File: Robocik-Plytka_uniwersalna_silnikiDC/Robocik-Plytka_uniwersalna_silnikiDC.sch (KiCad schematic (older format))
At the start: 48 parts, among them IC1 ACSL-6400-00TE, IC3 L6205D, J1 Conn_01x02, J2 ENG, J3 Conn_01x02, Q1 Q_NPN_BCE, Q2 Q_NPN_BCE, Q3 Q_NPN_BCE, U1 STM32F103C8Tx, U2 LD1117S33TR_SOT223, U3 L78L05_SOT89

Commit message: Added CAN transceiver schematic, Boot and LSE/OSC oscillator schematic, updated drawing. Added MCU pinout from STM32CubeMX
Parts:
- added C? (x4): 100nF, symbol Device:C_Small
- added J2: Tryb, Connector_PinHeader_2.54mm:PinHeader_1x03_P2.54mm_Vertical, symbol Connector:Conn_01x03_Male
- added J3: Magistrala_CAN, Connector_PinHeader_2.54mm:PinHeader_1x02_P2.54mm_Vertical, symbol Connector:Conn_01x02_Male
- added JP1: Zworka, Connector_PinHeader_2.54mm:PinHeader_1x02_P2.54mm_Vertical, symbol Device:Jumper_NO_Small
- added R1: 10k, Resistor_SMD:R_1206_3216Metric, symbol Device:R_Small
- added R2: 2k2, Resistor_SMD:R_1206_3216Metric, symbol Device:R_Small
- added R3: 120R, Resistor_SMD:R_1206_3216Metric, symbol Device:R
- added R? (x4): 10k, symbol Device:R_Small
- added SW?: SW_SPDT, symbol Switch:SW_SPDT
- added U1: SN65HVD230, Package_SO:SOIC-8_3.9x4.9mm_P1.27mm, symbol Interface_CAN_LIN:SN65HVD230
- added Y?: HSE OSC, symbol Device:Crystal_Small
- added Y?: LSE OSC, symbol Device:Crystal_Small
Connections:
- net labels added: BOOT0, GND, Pin_D, Pin_R
- wire segments 166 -> 213
- no-connect marks 0 -> 2
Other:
- note added: "Terminator podłączany na początku i na końcu magistrali"
- moved on the sheet: C?, R?

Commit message: Changed transceiver ground to digital, fixed power ground labelson driver ground, added footprints for capacitors and resistors.
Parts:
- C1, C10, C11, C12, C2, C3, C4, C5, C6, C7, C8, C9: renamed from C?; footprint (none) -> Capacitor_SMD:C_1206_3216Metric
- C13: renamed from C7; footprint (none) -> Capacitor_SMD:C_1206_3216Metric
- C14: renamed from C8; footprint (none) -> Capacitor_SMD:C_1206_3216Metric
- C15: renamed from C11; footprint (none) -> Capacitor_SMD:C_1206_3216Metric
- C16: renamed from C4; footprint (none) -> Capacitor_SMD:C_1206_3216Metric
- C17: renamed from C3; footprint (none) -> Capacitor_SMD:C_1206_3216Metric
- C18: renamed from C9; footprint (none) -> Capacitor_SMD:C_1206_3216Metric
- C19: renamed from C5; footprint (none) -> Capacitor_SMD:C_1206_3216Metric
- C20: renamed from C10; footprint (none) -> Capacitor_SMD:C_1206_3216Metric
- C21: renamed from C1; footprint (none) -> Capacitor_SMD:C_1206_3216Metric
- C22: renamed from C2; footprint (none) -> Capacitor_SMD:CP_Elec_6.3x5.8
- C23: renamed from C6; footprint (none) -> Capacitor_SMD:C_1206_3216Metric
- C24: renamed from C12; footprint (none) -> Capacitor_SMD:C_1206_3216Metric
- D1, D2: footprint (none) -> Diode_SMD:D_SOD-123
- R1, R14, R15, R17, R2, R3, R4, R5: renamed from R?; footprint (none) -> Resistor_SMD:R_1206_3216Metric
- R11: renamed from R9; footprint (none) -> Resistor_SMD:R_1206_3216Metric
- R12: renamed from R10; footprint (none) -> Resistor_SMD:R_1206_3216Metric
- R13: renamed from R11; footprint (none) -> Resistor_SMD:R_1206_3216Metric
- R19: renamed from R16; footprint (none) -> Resistor_SMD:R_1206_3216Metric
- R20: renamed from R15; footprint (none) -> Resistor_SMD:R_1206_3216Metric
- R21: renamed from R17; footprint (none) -> Resistor_SMD:R_1206_3216Metric
- R6: renamed from R1; footprint (none) -> Resistor_SMD:R_1206_3216Metric
- R7: renamed from R2; footprint (none) -> Resistor_SMD:R_1206_3216Metric
- R8: renamed from R5; footprint (none) -> Resistor_SMD:R_1206_3216Metric
- R9: renamed from R6; footprint (none) -> Resistor_SMD:R_1206_3216Metric
- gave numbers to parts that had none: 4
- renumbered IC3 to IC2, J2 to J1, J1 to J4, J2 to J5, J3 to J6, R2 to R10, R1 to R16, R3 to R18, U1 to U2, U2 to U3, U3 to U4
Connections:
- net labels removed: GND, VssPWR
- wire segments 213 -> 218
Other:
- moved on the sheet: C21, C22

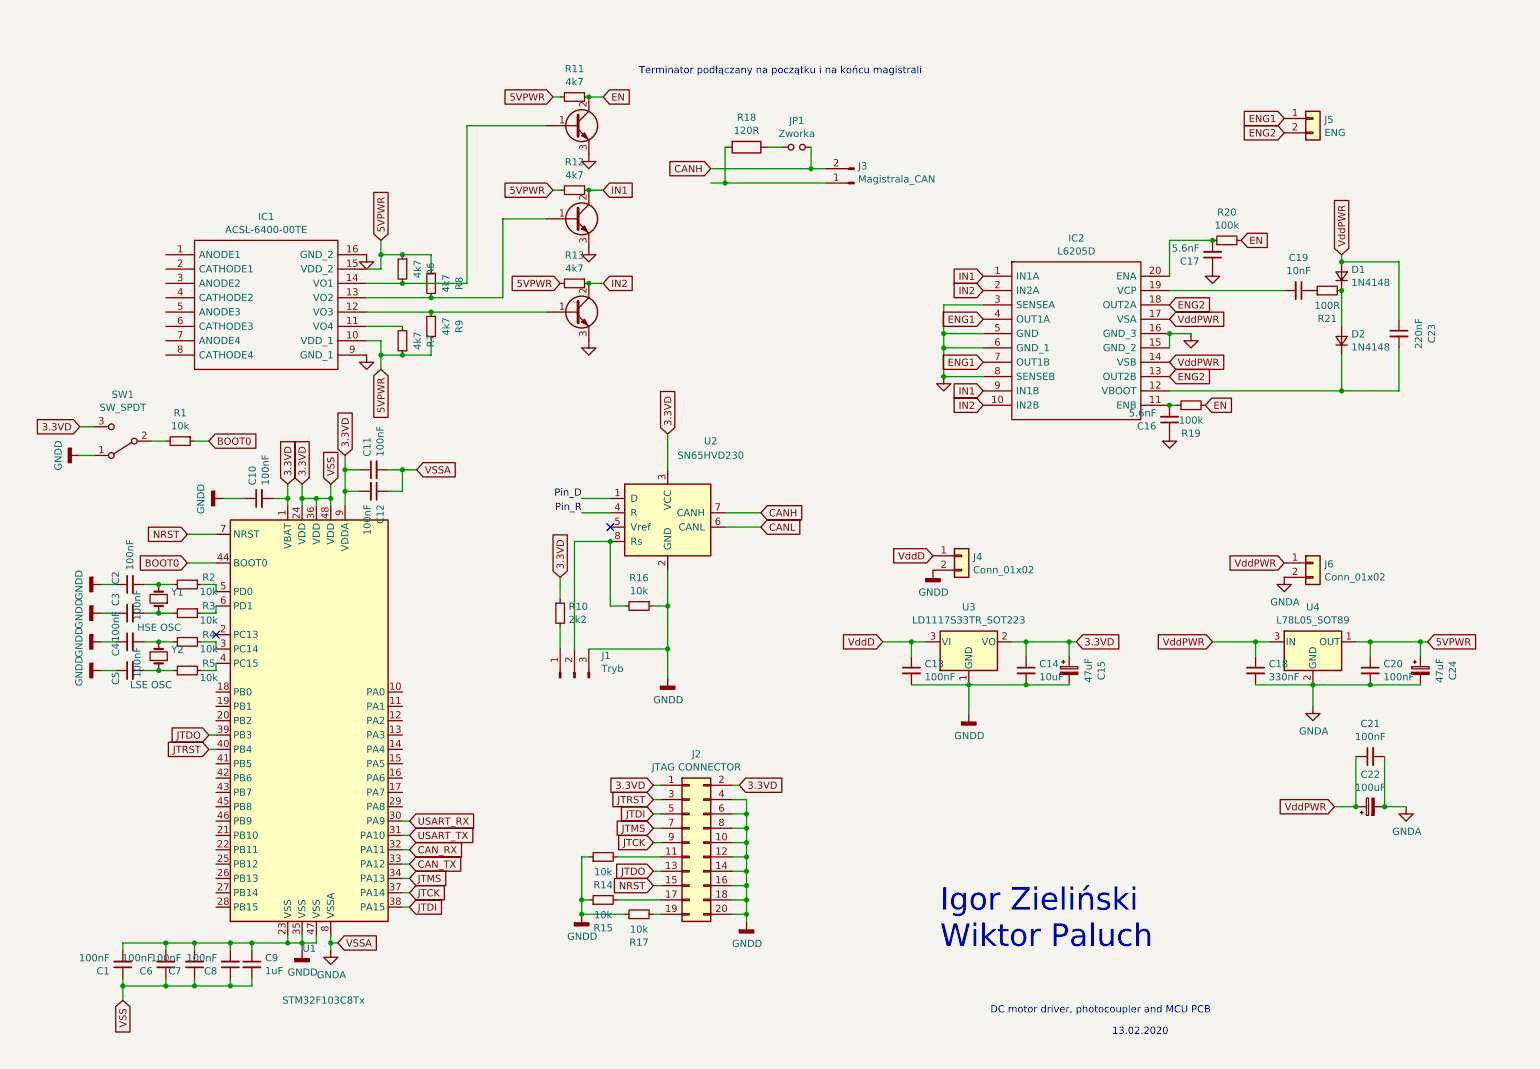
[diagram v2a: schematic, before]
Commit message: Schematic: Changed programming from JTAG to SWD. Added solderbridges. Added timers and their connections with optocoupler. Corrected minor mistakes. PCB: First version: organised elements, most connections are done.
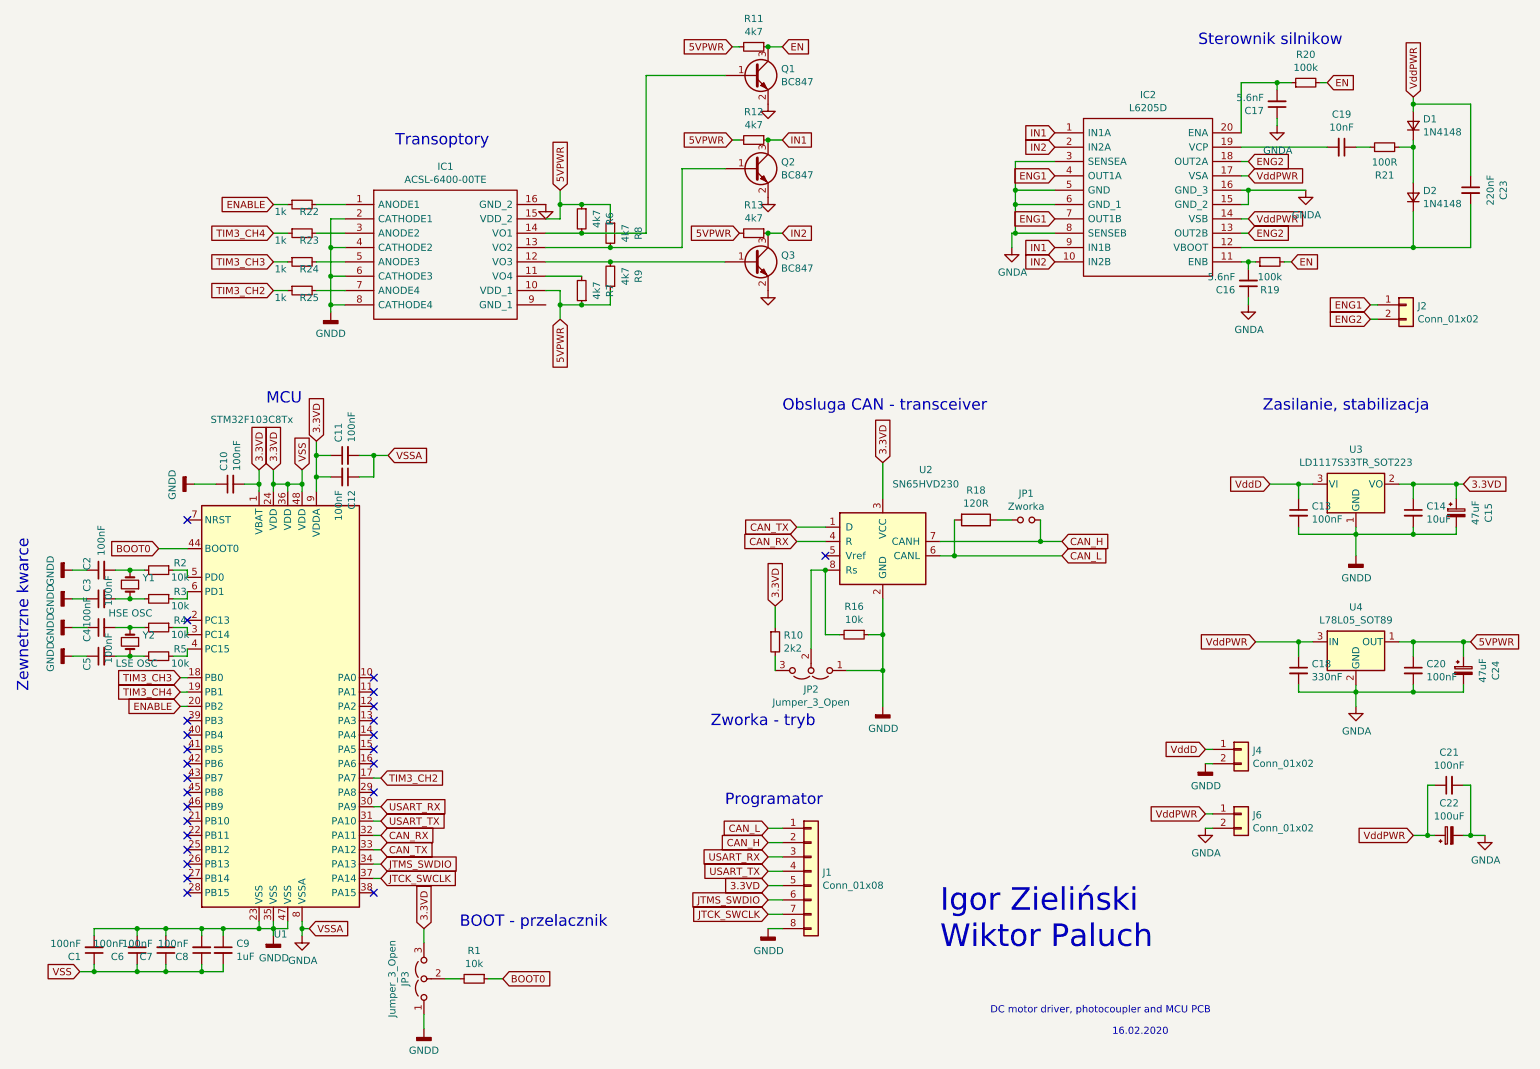
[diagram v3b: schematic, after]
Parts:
- removed J1: Tryb, Connector_PinHeader_2.54mm:PinHeader_1x03_P2.54mm_Vertical, symbol Connector:Conn_01x03_Male
- removed J2: JTAG CONNECTOR, symbol Connector_Generic:Conn_02x10_Odd_Even
- removed J3: Magistrala_CAN, Connector_PinHeader_2.54mm:PinHeader_1x02_P2.54mm_Vertical, symbol Connector:Conn_01x02_Male
- removed J5: ENG, symbol Connector_Generic:Conn_01x02
- removed Q1, Q2, Q3: Q_NPN_BCE, symbol Device:Q_NPN_BCE
- removed R14, R15, R17: 10k, Resistor_SMD:R_1206_3216Metric, symbol Device:R_Small
- removed SW1: SW_SPDT, symbol Switch:SW_SPDT
- added J1: Conn_01x08, Connector_PinHeader_2.54mm:PinHeader_1x08_P2.54mm_Vertical, symbol Connector_Generic:Conn_01x08
- added J2: Conn_01x02, Connector_PinHeader_2.54mm:PinHeader_1x02_P2.54mm_Vertical, symbol Connector_Generic:Conn_01x02
- added JP2, JP3: Jumper_3_Open, Jumper:SolderJumper-3_P1.3mm_Open_Pad1.0x1.5mm_NumberLabels, symbol Jumper:Jumper_3_Open
- added Q1, Q2, Q3: BC847, Package_TO_SOT_SMD:SOT-23, symbol Transistor_BJT:BC847
- added R22, R23, R24, R25: 1k, Resistor_SMD:R_1206_3216Metric, symbol Device:R_Small
- IC1: footprint SOIC127P599X173-16N -> Package_SO:SOP-16_4.55x10.3mm_P1.27mm
- IC2: footprint SOIC127P1032X265-20N -> Package_SO:SO-20_12.8x7.5mm_P1.27mm
- J4, J6: footprint (none) -> Connector_PinHeader_2.54mm:PinHeader_1x02_P2.54mm_Vertical
- JP1: footprint Connector_PinHeader_2.54mm:PinHeader_1x02_P2.54mm_Vertical -> Jumper:SolderJumper-2_P1.3mm_Open_Pad1.0x1.5mm
- Y1, Y2: footprint (none) -> Crystal:Crystal_SMD_5032-2Pin_5.0x3.2mm
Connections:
- net CANL is gone; now on net CAN_L: U2.6 (CANL)
- net Pin_D is gone; now on net CAN_TX: U2.1 (D)
- net Pin_R is gone; now on net CAN_RX: U2.4 (R)
- net 3.3VD: now also J1.5 (Pin_5), JP3.3 (B)
- net EN: now also Q1.3 (C)
- net ENG1: now also J2.1 (Pin_1)
- net ENG2: now also J2.2 (Pin_2)
- net GNDA: now also Q1.2 (E), Q2.2 (E), Q3.2 (E); no longer IC1.9 (GND_1)
- net GNDD: now also IC1.2 (CATHODE1), IC1.4 (CATHODE2), IC1.6 (CATHODE3), IC1.8 (CATHODE4), J1.8 (Pin_8), JP2.1 (A), JP3.1 (A)
- net IN1: now also Q2.3 (C)
- net IN2: now also Q3.3 (C)
- net USART_RX: now also J1.3 (Pin_3)
- net USART_TX: now also J1.4 (Pin_4)
- net at R16.2, U2.8 (Rs): now also JP2.2 (C)
- net CAN_L: now reaches R18.2
- net CAN_L: now also J1.1 (Pin_1)
- net at R10.2: now also JP2.3 (B)
- net at IC1.1 (ANODE1): now also R22.2
- net at IC1.12 (VO3), R9.2: now also Q3.1 (B)
- net at IC1.13 (VO2), R8.2: now also Q2.1 (B)
- net at IC1.14 (VO1), R6.2: now also Q1.1 (B)
- net at IC1.3 (ANODE2): now also R23.2
- net at IC1.5 (ANODE3): now also R24.2
- net at IC1.7 (ANODE4): now also R25.2
- net TIM3_CH2: now reaches U1.17 (PA7)
- net TIM3_CH2: now also R25.1
- net TIM3_CH3: now reaches U1.18 (PB0)
- net TIM3_CH3: now also R24.1
- net TIM3_CH4: now reaches U1.19 (PB1)
- net TIM3_CH4: now also R23.1
- net ENABLE: now reaches U1.20 (PB2)
- net ENABLE: now also R22.1
- net at R1.2: now also JP3.2 (C)
- net CANH renamed CAN_H
- net CAN_H: now also J1.2 (Pin_2)
- net JTCK renamed JTCK_SWCLK
- net JTCK_SWCLK: now also J1.7 (Pin_7)
- net JTDI: no longer names the net of U1.38 (PA15)
- net JTDO: no longer names the net of U1.39 (PB3)
- net JTMS renamed JTMS_SWDIO
- net JTMS_SWDIO: now also J1.6 (Pin_6)
- net JTRST: no longer names the net of U1.40 (PB4)
- net NRST: no longer names the net of U1.7 (NRST)
- no-connect marks 2 -> 25
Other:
- note added: "16.02.2020"
- note added: "BOOT - przelacznik"
- note added: "MCU"
- note added: "Obsluga CAN - transceiver"
- note added: "Programator"
- note added: "Sterownik silnikow"
- note added: "Transoptory"
- note added: "Zasilanie, stabilizacja"
- note added: "Zewnetrzne kwarce"
- note added: "Zworka - tryb"
- note removed: "13.02.2020"
- note removed: "Terminator podłączany na początku i na końcu magistrali"
- moved on the sheet: C1, C10, C11, C12, C13, C14, C15, C16, C17, C18, C19, C2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

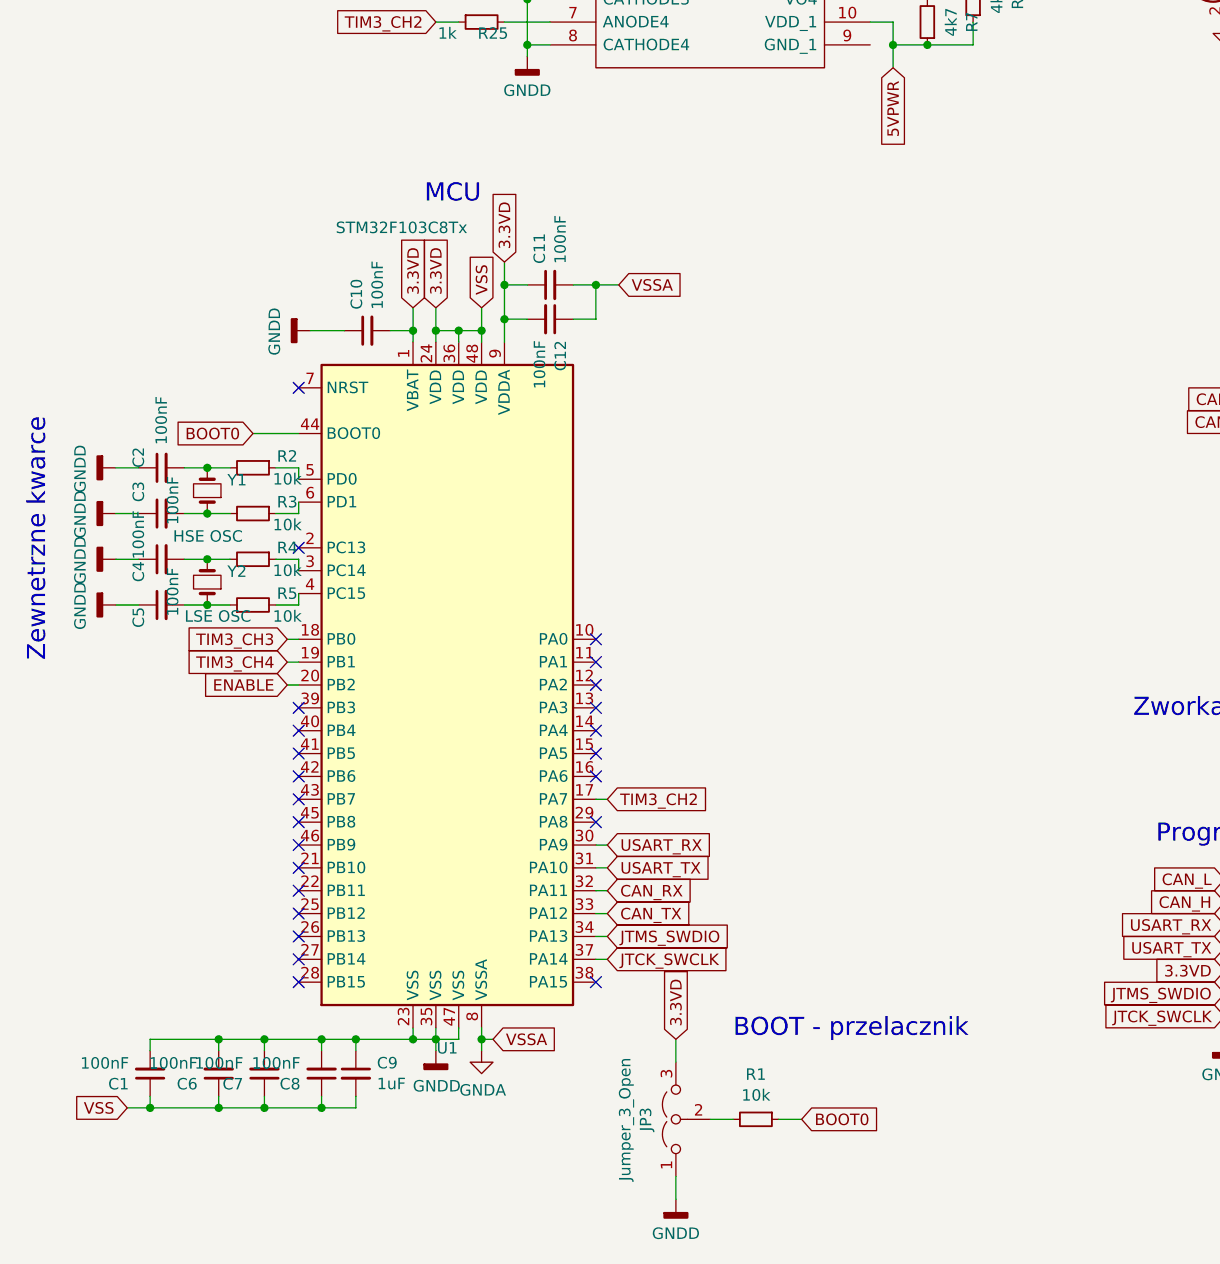
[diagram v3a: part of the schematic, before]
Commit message: Changed power supply line on schematic, added missing connections on PCB layout, added second layer connections and vias. Added layout drawing and updated schematic drawing
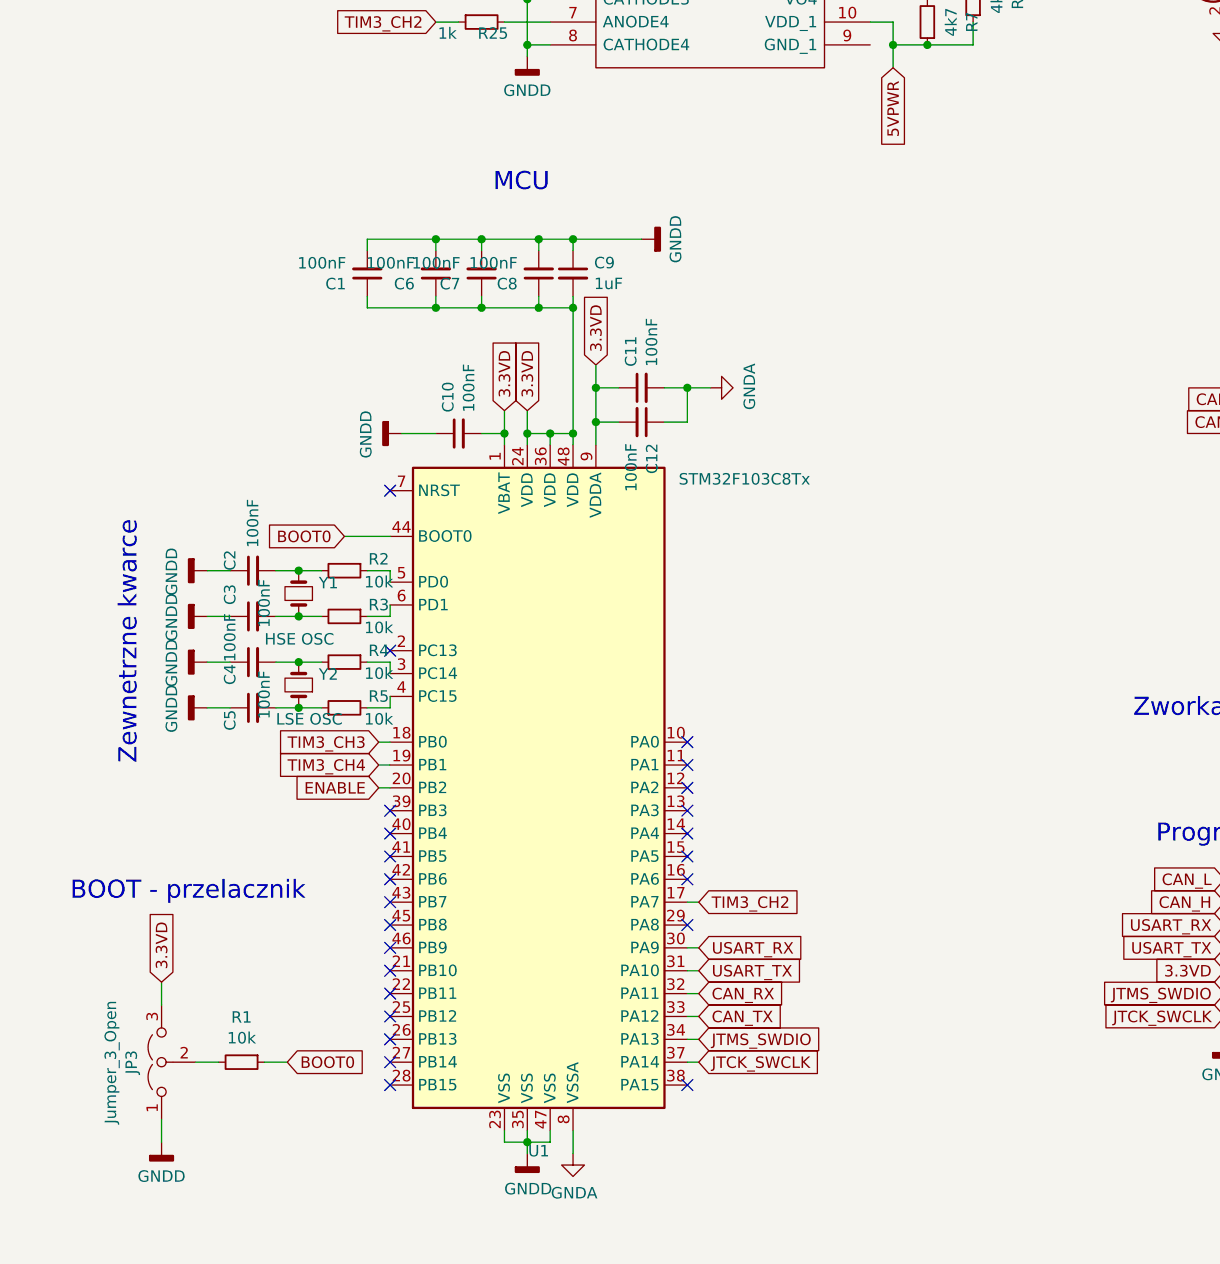
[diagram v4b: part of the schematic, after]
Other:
- moved on the sheet: C1, C10, C11, C12, C2, C3, C4, C5, C6, C7, C8, C9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
